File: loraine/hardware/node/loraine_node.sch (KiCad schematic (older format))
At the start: 53 parts, among them CON1 BARREL_JACK, IC1 ATTINY2313A-S, K1 LED1, K2 LED2, K3 LED3, P1 POWER_THRU, P2 POWER, P3 SOLDER_PAD, P4 BUS, P5 BUS_THRU, P6 ICSP, P7 OUTPUTS, Q1 TSM3460CX6, Q2 TSM3460CX6, Q3 TSM3460CX6, Q4 TSM3460CX6, Q5 TSM3460CX6, Q6 TSM3460CX6, Q7 TSM3460CX6, Q8 TSM3460CX6, U1 UA7805CKCT, U2 SN65176BD, X1 16MHz

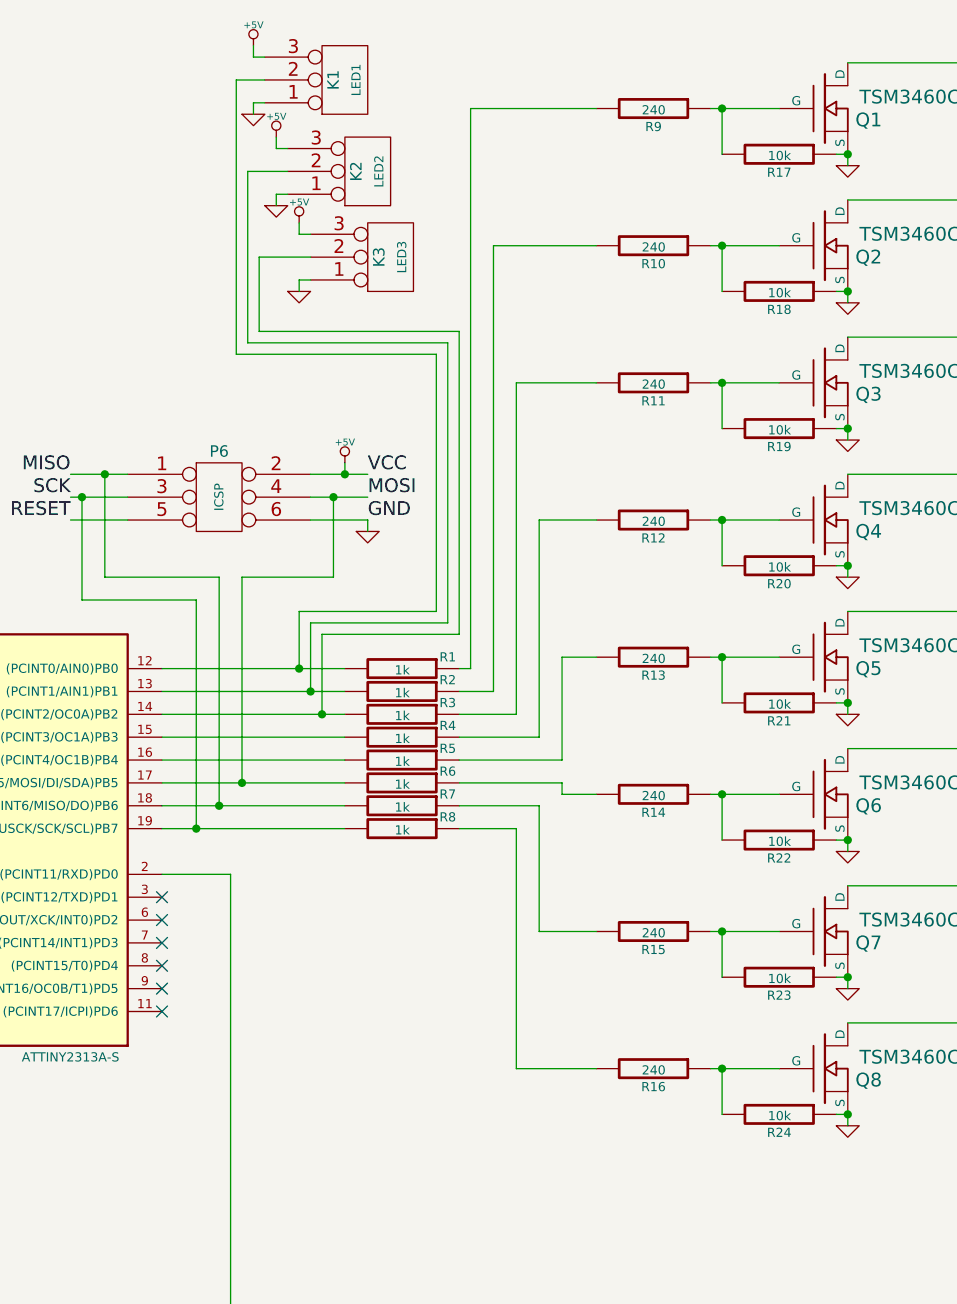
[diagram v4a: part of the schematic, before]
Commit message: Finished footprint placement on node board
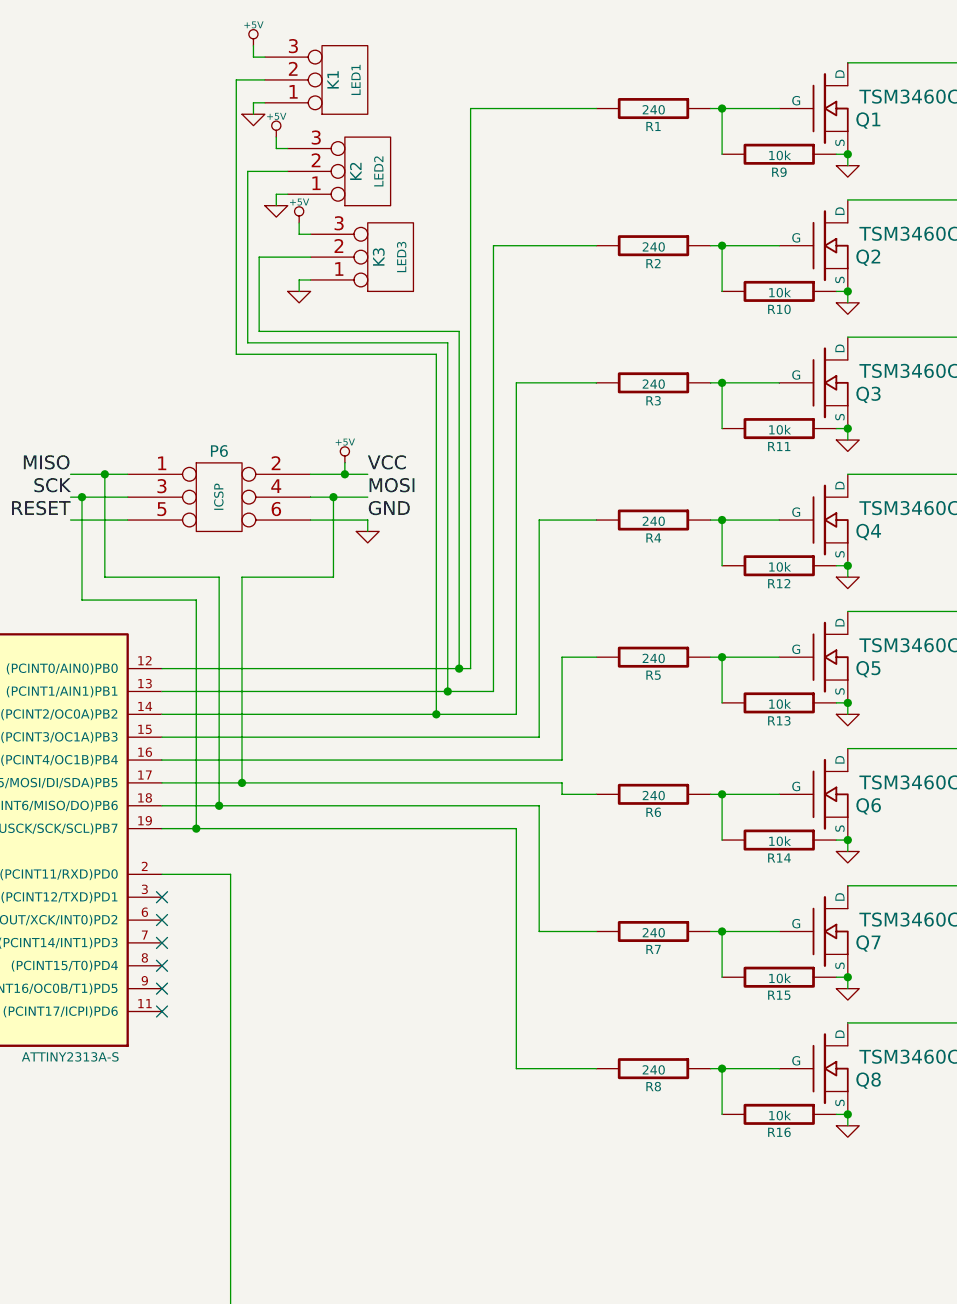
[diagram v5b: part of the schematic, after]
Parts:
- removed R1, R2, R3, R4, R5, R6, R7, R8: 1k, SMD_Packages:SM0805, symbol R
- renumbered R9 to R1, R18 to R10, R19 to R11, R20 to R12, R21 to R13, R22 to R14, R23 to R15, R24 to R16, R10 to R2, R11 to R3, R12 to R4, R13 to R5, R14 to R6, R15 to R7, R16 to R8, R17 to R9
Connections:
- net MISO: now also R7.2
- net MOSI: now also R6.2
- net SCK: now also R8.2
- net at IC1.12 ((PCINT0/AIN0)PB0): now also K3.2 (PM), R1.2; no longer K1.2 (PM)
- net at IC1.13 ((PCINT1/AIN1)PB1), K2.2 (PM): now also R2.2
- net at IC1.14 ((PCINT2/OC0A)PB2): now also K1.2 (PM), R3.2; no longer K3.2 (PM)
- net at IC1.15 ((PCINT3/OC1A)PB3): now also R4.2
- net at IC1.16 ((PCINT4/OC1B)PB4): now also R5.2
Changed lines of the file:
@@
-$EndComp
-$Comp
-L R R1
-U 1 1 533877F8
-P 5850 3650
-F 0 "R1" V 5800 3850 40  0000 C CNN
-F 1 "1k" V 5857 3651 40  0000 C CNN
-F 2 "SMD_Packages:SM0805" V 5780 3650 30  0001 C CNN
-F 3 "" H 5850 3650 30  0000 C CNN
-	1    5850 3650
-	0    1    1    0
 $EndComp
 $Comp
@@
 	1    3600 1350
 	1    0    0    -1
-$EndComp
-$Comp
-L R R2
-U 1 1 53387FC9
-P 5850 3750
-F 0 "R2" V 5800 3950 40  0000 C CNN
-F 1 "1k" V 5857 3751 40  0000 C CNN
-F 2 "SMD_Packages:SM0805" V 5780 3750 30  0001 C CNN
-F 3 "" H 5850 3750 30  0000 C CNN
-	1    5850 3750
-	0    1    1    0
-$EndComp
-$Comp
-L R R3
-U 1 1 53387FDD
-P 5850 3850
-F 0 "R3" V 5800 4050 40  0000 C CNN
-F 1 "1k" V 5857 3851 40  0000 C CNN
-F 2 "SMD_Packages:SM0805" V 5780 3850 30  0001 C CNN
-F 3 "" H 5850 3850 30  0000 C CNN
-	1    5850 3850
-	0    1    1    0
-$EndComp
-$Comp
-L R R4
-U 1 1 53387FF1
-P 5850 3950
-F 0 "R4" V 5800 4150 40  0000 C CNN
-F 1 "1k" V 5857 3951 40  0000 C CNN
-F 2 "SMD_Packages:SM0805" V 5780 3950 30  0001 C CNN
-F 3 "" H 5850 3950 30  0000 C CNN
-	1    5850 3950
-	0    1    1    0
-$EndComp
-$Comp
-L R R5
-U 1 1 53388005
-P 5850 4050
-F 0 "R5" V 5800 4250 40  0000 C CNN
-F 1 "1k" V 5857 4051 40  0000 C CNN
-F 2 "SMD_Packages:SM0805" V 5780 4050 30  0001 C CNN
-F 3 "" H 5850 4050 30  0000 C CNN
-	1    5850 4050
-	0    1    1    0
-$EndComp
-$Comp
-L R R6
-U 1 1 53388019
-P 5850 4150
-F 0 "R6" V 5800 4350 40  0000 C CNN
-F 1 "1k" V 5857 4151 40  0000 C CNN
-F 2 "SMD_Packages:SM0805" V 5780 4150 30  0001 C CNN
-F 3 "" H 5850 4150 30  0000 C CNN
-	1    5850 4150
-	0    1    1    0
-$EndComp
-$Comp
-L R R7
-U 1 1 5338802D
-P 5850 4250
-F 0 "R7" V 5800 4450 40  0000 C CNN
-F 1 "1k" V 5857 4251 40  0000 C CNN
-F 2 "SMD_Packages:SM0805" V 5780 4250 30  0001 C CNN
-F 3 "" H 5850 4250 30  0000 C CNN
-	1    5850 4250
-	0    1    1    0
-$EndComp
-$Comp
-L R R8
-U 1 1 53388041
-P 5850 4350
-F 0 "R8" V 5800 4550 40  0000 C CNN
-F 1 "1k" V 5857 4351 40  0000 C CNN
-F 2 "SMD_Packages:SM0805" V 5780 4350 30  0001 C CNN
-F 3 "" H 5850 4350 30  0000 C CNN
-	1    5850 4350
-	0    1    1    0
 $EndComp
 $Comp
@@
 Connection ~ 2200 1150
 Wire Wire Line
-	4800 3650 5600 3650
-Wire Wire Line
-	4800 3750 5600 3750
-Wire Wire Line
-	4800 3850 5600 3850
-Wire Wire Line
-	4800 3950 5600 3950
-Wire Wire Line
-	4800 4050 5600 4050
-Wire Wire Line
-	4800 4150 5600 4150
-Wire Wire Line
-	4800 4250 5600 4250
-Wire Wire Line
-	4800 4350 5600 4350
-Wire Wire Line
-	6150 3650 6100 3650
-Wire Wire Line
-	6250 3750 6100 3750
-Wire Wire Line
-	6350 3850 6100 3850
-Wire Wire Line
-	6450 3950 6100 3950
-Wire Wire Line
-	6450 3000 6450 3950
-Wire Wire Line
-	6100 4350 6350 4350
+	4800 3650 6150 3650
+Wire Wire Line
+	4800 3850 6350 3850
+Wire Wire Line
+	4800 3950 6450 3950
+Wire Wire Line
+	4800 4050 6550 4050
+Wire Wire Line
+	4800 4150 6550 4150
+Wire Wire Line
+	4800 4250 6450 4250
+Wire Wire Line
+	4800 4350 6350 4350
+Wire Wire Line
+	6450 3950 6450 3000
 Wire Wire Line
 	4450 7000 4750 7000
@@
 Connection ~ 2900 7200
 Wire Wire Line
-	6150 1200 6150 3650
-Wire Wire Line
-	6250 1800 6250 3750
-Wire Wire Line
-	6350 2400 6350 3850
-Wire Wire Line
-	5500 3850 5500 3500
-Wire Wire Line
-	5500 3500 6100 3500
-Connection ~ 5500 3850
-Wire Wire Line
-	5450 3750 5450 3450
-Wire Wire Line
-	5450 3450 6050 3450
-Connection ~ 5450 3750
-Wire Wire Line
-	5400 3650 5400 3400
-Wire Wire Line
-	5400 3400 6000 3400
-Connection ~ 5400 3650
+	6150 3650 6150 1200
+Wire Wire Line
+	6250 3750 6250 1800
+Wire Wire Line
+	6350 3850 6350 2400
 Wire Wire Line
 	3500 3200 3450 3200
@@
 $EndComp
 $Comp
-L R R9
+L R R1
 U 1 1 53C70B69
 P 6950 1200
-F 0 "R9" V 7030 1200 40  0000 C CNN
+F 0 "R1" V 7030 1200 40  0000 C CNN
 F 1 "240" V 6957 1201 40  0000 C CNN
 F 2 "SMD_Packages:SM0805" V 6880 1200 30  0001 C CNN
@@
 	5225 2175 6100 2175
 Wire Wire Line
-	6100 2175 6100 3500
-Wire Wire Line
-	6050 3450 6050 2225
+	6100 2175 6100 3650
+Wire Wire Line
+	6050 2225 6050 3750
 Wire Wire Line
 	6050 2225 5175 2225
@@
 	5125 2275 6000 2275
 Wire Wire Line
-	6000 2275 6000 3400
-$Comp
-L R R17
+	6000 2275 6000 3850
+$Comp
+L R R9
 U 1 1 53C70202
 P 7500 1400
-F 0 "R17" V 7580 1400 40  0000 C CNN
+F 0 "R9" V 7580 1400 40  0000 C CNN
 F 1 "10k" V 7507 1401 40  0000 C CNN
 F 2 "SMD_Packages:SM0805" V 7430 1400 30  0001 C CNN
@@
 $EndComp
 $Comp
-L R R10
+L R R2
 U 1 1 53CC8837
 P 6950 1800
-F 0 "R10" V 7030 1800 40  0000 C CNN
+F 0 "R2" V 7030 1800 40  0000 C CNN
 F 1 "240" V 6957 1801 40  0000 C CNN
 F 2 "SMD_Packages:SM0805" V 6880 1800 30  0001 C CNN
@@
 Connection ~ 7800 2000
 $Comp
-L R R18
+L R R10
 U 1 1 53CC8841
 P 7500 2000
-F 0 "R18" V 7580 2000 40  0000 C CNN
+F 0 "R10" V 7580 2000 40  0000 C CNN
 F 1 "10k" V 7507 2001 40  0000 C CNN
 F 2 "SMD_Packages:SM0805" V 7430 2000 30  0001 C CNN
@@
 $EndComp
 $Comp
-L R R11
+L R R3
 U 1 1 53CC8B2F
 P 6950 2400
-F 0 "R11" V 7030 2400 40  0000 C CNN
+F 0 "R3" V 7030 2400 40  0000 C CNN
 F 1 "240" V 6957 2401 40  0000 C CNN
 F 2 "SMD_Packages:SM0805" V 6880 2400 30  0001 C CNN
@@
 Connection ~ 7800 2600
 $Comp
-L R R19
+L R R11
 U 1 1 53CC8B39
 P 7500 2600
-F 0 "R19" V 7580 2600 40  0000 C CNN
+F 0 "R11" V 7580 2600 40  0000 C CNN
 F 1 "10k" V 7507 2601 40  0000 C CNN
 F 2 "SMD_Packages:SM0805" V 7430 2600 30  0001 C CNN
@@
 $EndComp
 $Comp
-L R R12
+L R R4
 U 1 1 53CC8D44
 P 6950 3000
-F 0 "R12" V 7030 3000 40  0000 C CNN
+F 0 "R4" V 7030 3000 40  0000 C CNN
 F 1 "240" V 6957 3001 40  0000 C CNN
 F 2 "SMD_Packages:SM0805" V 6880 3000 30  0001 C CNN
@@
 Connection ~ 7800 3200
 $Comp
-L R R20
+L R R12
 U 1 1 53CC8D4E
 P 7500 3200
-F 0 "R20" V 7580 3200 40  0000 C CNN
+F 0 "R12" V 7580 3200 40  0000 C CNN
 F 1 "10k" V 7507 3201 40  0000 C CNN
 F 2 "SMD_Packages:SM0805" V 7430 3200 30  0001 C CNN
@@
 $EndComp
 $Comp
-L R R13
+L R R5
 U 1 1 53CC8F3B
 P 6950 3600
-F 0 "R13" V 7030 3600 40  0000 C CNN
+F 0 "R5" V 7030 3600 40  0000 C CNN
 F 1 "240" V 6957 3601 40  0000 C CNN
 F 2 "SMD_Packages:SM0805" V 6880 3600 30  0001 C CNN
@@
 Connection ~ 7800 3800
 $Comp
-L R R21
+L R R13
 U 1 1 53CC8F45
 P 7500 3800
-F 0 "R21" V 7580 3800 40  0000 C CNN
+F 0 "R13" V 7580 3800 40  0000 C CNN
 F 1 "10k" V 7507 3801 40  0000 C CNN
 F 2 "SMD_Packages:SM0805" V 7430 3800 30  0001 C CNN
@@
 $EndComp
 $Comp
-L R R14
+L R R6
 U 1 1 53CC9380
 P 6950 4200
-F 0 "R14" V 7030 4200 40  0000 C CNN
+F 0 "R6" V 7030 4200 40  0000 C CNN
 F 1 "240" V 6957 4201 40  0000 C CNN
 F 2 "SMD_Packages:SM0805" V 6880 4200 30  0001 C CNN
@@
 Connection ~ 7800 4400
 $Comp
-L R R22
+L R R14
 U 1 1 53CC938A
 P 7500 4400
-F 0 "R22" V 7580 4400 40  0000 C CNN
+F 0 "R14" V 7580 4400 40  0000 C CNN
 F 1 "10k" V 7507 4401 40  0000 C CNN
 F 2 "SMD_Packages:SM0805" V 7430 4400 30  0001 C CNN
@@
 $EndComp
 $Comp
-L R R15
+L R R7
 U 1 1 53CC9890
 P 6950 4800
-F 0 "R15" V 7030 4800 40  0000 C CNN
+F 0 "R7" V 7030 4800 40  0000 C CNN
 F 1 "240" V 6957 4801 40  0000 C CNN
 F 2 "SMD_Packages:SM0805" V 6880 4800 30  0001 C CNN
@@
 Connection ~ 7800 5000
 $Comp
-L R R23
+L R R15
 U 1 1 53CC989A
 P 7500 5000
-F 0 "R23" V 7580 5000 40  0000 C CNN
+F 0 "R15" V 7580 5000 40  0000 C CNN
 F 1 "10k" V 7507 5001 40  0000 C CNN
 F 2 "SMD_Packages:SM0805" V 7430 5000 30  0001 C CNN
@@
 $EndComp
 $Comp
-L R R16
+L R R8
 U 1 1 53CC9B16
 P 6950 5400
-F 0 "R16" V 7030 5400 40  0000 C CNN
+F 0 "R8" V 7030 5400 40  0000 C CNN
 F 1 "240" V 6957 5401 40  0000 C CNN
 F 2 "SMD_Packages:SM0805" V 6880 5400 30  0001 C CNN
@@
 Connection ~ 7800 5600
 $Comp
-L R R24
+L R R16
 U 1 1 53CC9B20
 P 7500 5600
-F 0 "R24" V 7580 5600 40  0000 C CNN
+F 0 "R16" V 7580 5600 40  0000 C CNN
 F 1 "10k" V 7507 5601 40  0000 C CNN
 F 2 "SMD_Packages:SM0805" V 7430 5600 30  0001 C CNN
@@
 	6550 3600 6700 3600
 Wire Wire Line
-	6100 4050 6550 4050
-Wire Wire Line
 	6550 4050 6550 3600
 Wire Wire Line
-	6100 4150 6550 4150
-Wire Wire Line
 	6550 4150 6550 4200
 Wire Wire Line
@@
 Wire Wire Line
 	6450 4800 6700 4800
-Wire Wire Line
-	6100 4250 6450 4250
 Wire Wire Line
 	6450 4250 6450 4800
@@
 	1    0    0    -1
 $EndComp
+Wire Wire Line
+	4800 3750 6250 3750
+Connection ~ 6100 3650
+Connection ~ 6050 3750
+Connection ~ 6000 3850
 $EndSCHEMATC

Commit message: Finished both PCBs apart from logos and checking
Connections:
- net +5V: no longer K1.3 (P3), K2.3 (P3), K3.3 (P3)
- net +12V renamed VIN
- net VIN: now also K1.3 (P3), K2.3 (P3), K3.3 (P3)
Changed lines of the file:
@@
-$EndComp
-$Comp
-L +12V #PWR08
-U 1 1 5339006C
-P 2200 1100
-F 0 "#PWR08" H 2200 1050 20  0001 C CNN
-F 1 "+12V" H 2200 1200 30  0000 C CNN
-F 2 "" H 2200 1100 60  0000 C CNN
-F 3 "" H 2200 1100 60  0000 C CNN
-	1    2200 1100
-	1    0    0    -1
-$EndComp
-$Comp
-L +12V #PWR09
-U 1 1 53390BA6
-P 10375 5300
-F 0 "#PWR09" H 10375 5250 20  0001 C CNN
-F 1 "+12V" H 10375 5400 30  0000 C CNN
-F 2 "" H 10375 5300 60  0000 C CNN
-F 3 "" H 10375 5300 60  0000 C CNN
-	1    10375 5300
-	1    0    0    -1
 $EndComp
 $Comp
@@
 	1950 3650 2100 3650
 Wire Wire Line
-	10375 5300 10375 6100
+	10375 5150 10375 6100
 Wire Wire Line
 	10375 5400 10225 5400
@@
 	3850 1150 3850 1100
 Wire Wire Line
-	2200 1100 2200 1150
+	2200 1025 2200 1150
 Wire Wire Line
 	3450 3150 3450 3350
@@
 $EndComp
 $Comp
-L +5V #PWR011
-U 1 1 537905D6
-P 5200 925
-F 0 "#PWR011" H 5200 1015 20  0001 C CNN
-F 1 "+5V" H 5200 1015 30  0000 C CNN
-F 2 "" H 5200 925 60  0000 C CNN
-F 3 "" H 5200 925 60  0000 C CNN
-	1    5200 925
-	1    0    0    -1
-$EndComp
-$Comp
-L +5V #PWR012
-U 1 1 5379060F
-P 5300 1325
-F 0 "#PWR012" H 5300 1415 20  0001 C CNN
-F 1 "+5V" H 5300 1415 30  0000 C CNN
-F 2 "" H 5300 1325 60  0000 C CNN
-F 3 "" H 5300 1325 60  0000 C CNN
-	1    5300 1325
-	1    0    0    -1
-$EndComp
-$Comp
-L +5V #PWR013
-U 1 1 53790648
-P 5400 1700
-F 0 "#PWR013" H 5400 1790 20  0001 C CNN
-F 1 "+5V" H 5400 1790 30  0000 C CNN
-F 2 "" H 5400 1700 60  0000 C CNN
-F 3 "" H 5400 1700 60  0000 C CNN
-	1    5400 1700
-	1    0    0    -1
-$EndComp
-$Comp
 L GND #PWR014
 U 1 1 53790927
@@
 	5300 1575 5350 1575
 Wire Wire Line
-	5300 1325 5300 1375
-Wire Wire Line
-	5300 1375 5350 1375
+	4750 1375 5350 1375
 Wire Wire Line
 	5200 1225 5200 1175
@@
 	5200 1175 5250 1175
 Wire Wire Line
-	5200 925  5200 975
-Wire Wire Line
-	5200 975  5250 975
-Wire Wire Line
-	5400 1700 5400 1750
-Wire Wire Line
-	5400 1750 5450 1750
+	4875 975  5250 975
+Wire Wire Line
+	4925 1750 5450 1750
 Wire Wire Line
 	5400 2000 5400 1950
@@
 Connection ~ 6050 3750
 Connection ~ 6000 3850
+Text GLabel 2250 1025 2    60   Input ~ 0
+VIN
+Wire Wire Line
+	2200 1025 2250 1025
+Text GLabel 4750 1375 0    60   Output ~ 0
+VIN
+Wire Wire Line
+	4875 1375 4875 975
+Connection ~ 4875 1375
+Wire Wire Line
+	4925 1375 4925 1750
+Connection ~ 4925 1375
+Text GLabel 10275 5150 0    60   Input ~ 0
+VIN
+Wire Wire Line
+	10275 5150 10375 5150
 $EndSCHEMATC

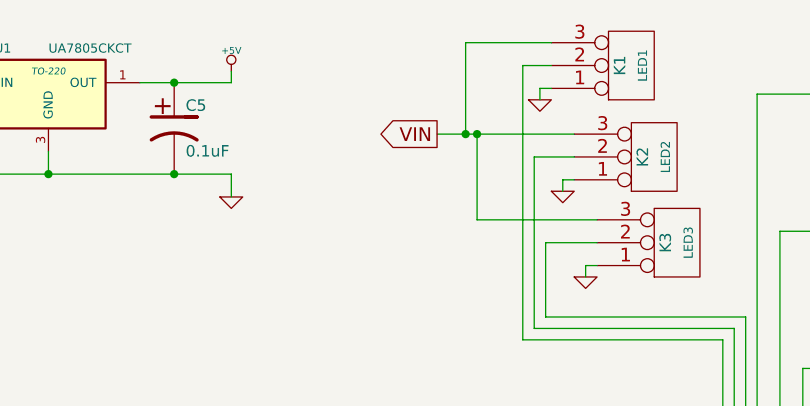
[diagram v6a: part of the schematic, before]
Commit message: 5V power conn on uplighter board
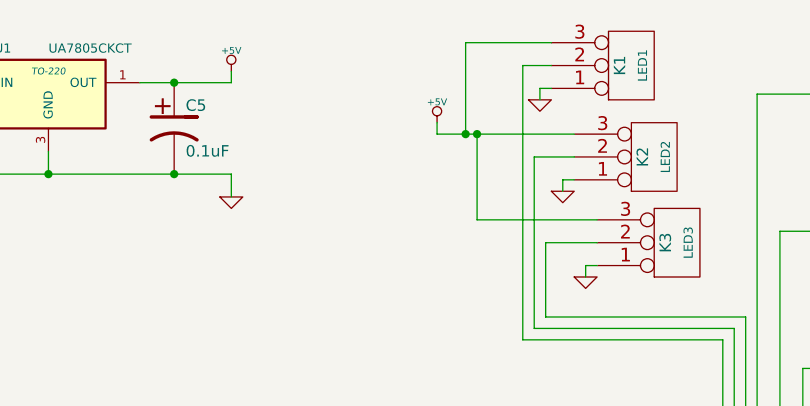
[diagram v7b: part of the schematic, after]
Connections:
- net +5V: now also K1.3 (P3), K2.3 (P3), K3.3 (P3)
- net VIN: no longer K1.3 (P3), K2.3 (P3), K3.3 (P3)
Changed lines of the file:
@@
 Wire Wire Line
 	2200 1025 2250 1025
-Text GLabel 4750 1375 0    60   Output ~ 0
-VIN
 Wire Wire Line
 	4875 1375 4875 975
@@
 Wire Wire Line
 	10275 5150 10375 5150
+$Comp
+L +5V #PWR?
+U 1 1 53CD6C0A
+P 4750 1325
+F 0 "#PWR?" H 4750 1415 20  0001 C CNN
+F 1 "+5V" H 4750 1415 30  0000 C CNN
+F 2 "" H 4750 1325 60  0000 C CNN
+F 3 "" H 4750 1325 60  0000 C CNN
+	1    4750 1325
+	1    0    0    -1
+$EndComp
+Wire Wire Line
+	4750 1325 4750 1375
 $EndSCHEMATC
